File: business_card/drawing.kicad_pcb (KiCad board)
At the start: 2 copper layers, 85.5 x 53.9 mm, 0 parts

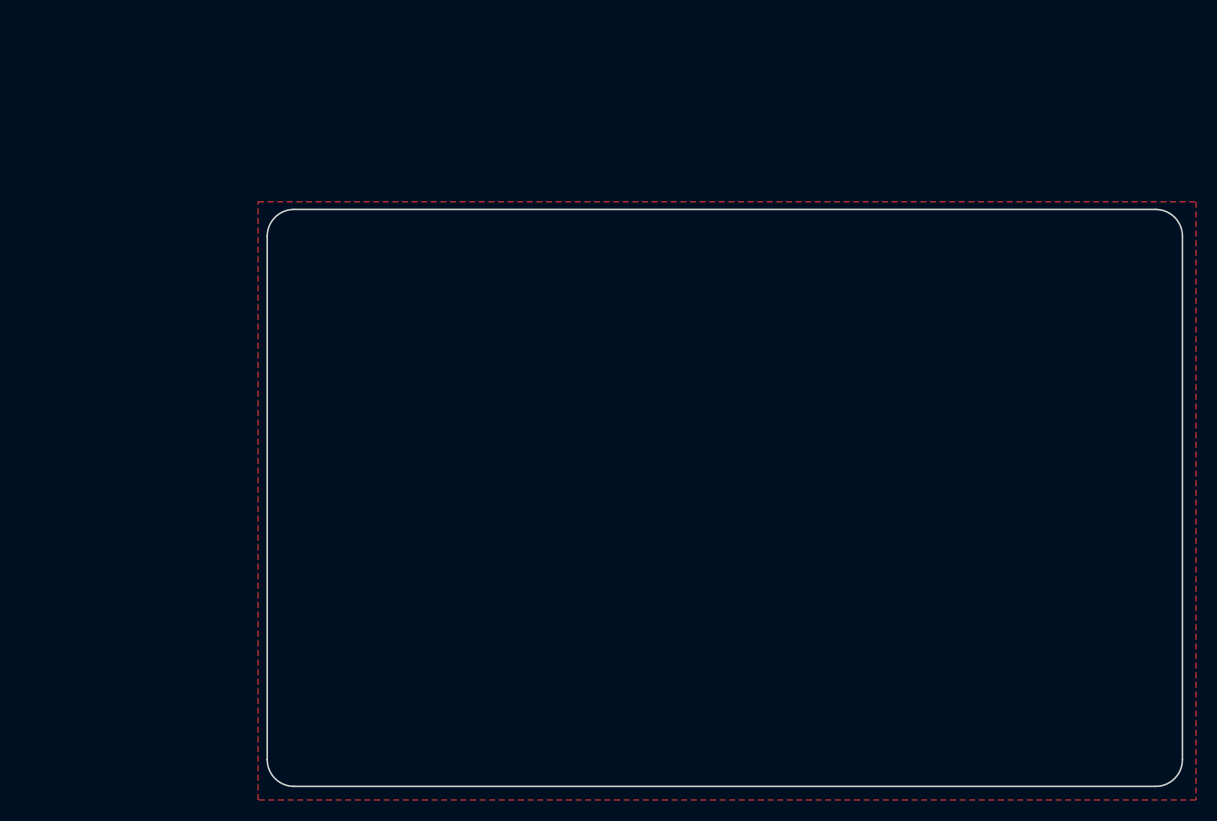
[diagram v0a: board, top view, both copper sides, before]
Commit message: feat[card]: worlds business card design
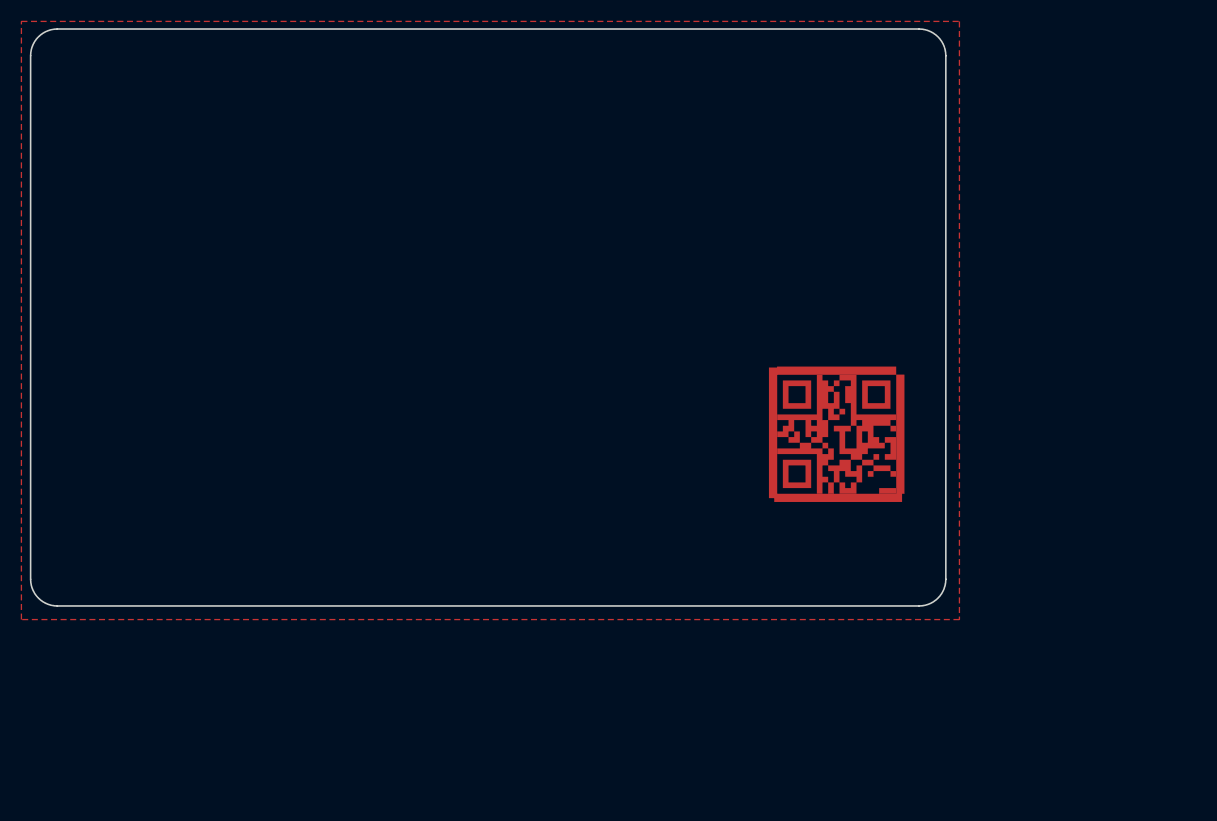
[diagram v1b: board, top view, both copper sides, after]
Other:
- board text added: "//ATTEMPT THE IMPOSSIBLE."
- board text added: "EMAIL:"
- board text added: "MRX.EE"
- board text added: "MRX@MRX.EE"
- board text added: "UNLEASH INNOVATION"
- board text added: "WEB:"
- board text removed: "> NFC ON BACK_"
- board text removed: "ATTEMPT THE IMPOSSIBLE."
- board text removed: "TAP PHONE TO OPEN"
